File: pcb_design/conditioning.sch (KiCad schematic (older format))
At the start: 17 parts

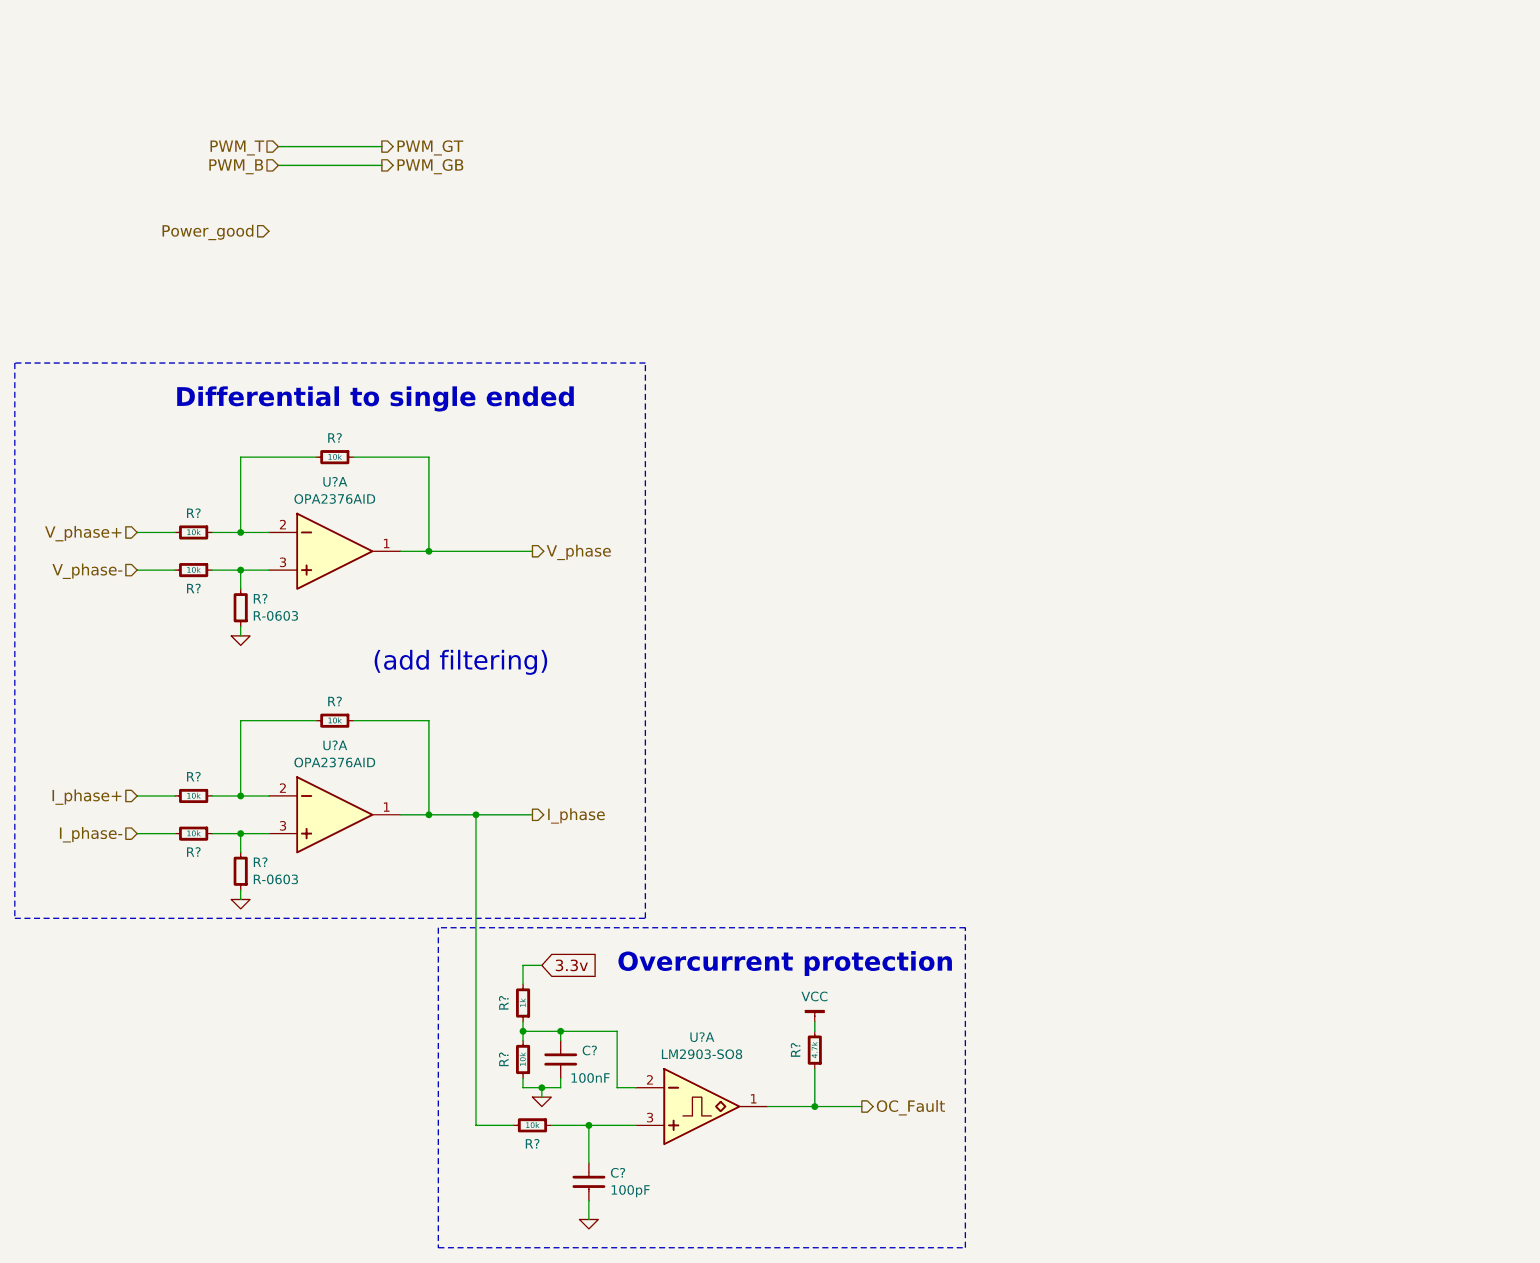
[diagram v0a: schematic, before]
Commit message: Updated MCU sheet to comply with VESC 6 pinout. Added 5v analog inputs and updated some labels
Signed-off-by: Marcos Chaparro <mchaparro@paltatech.com>
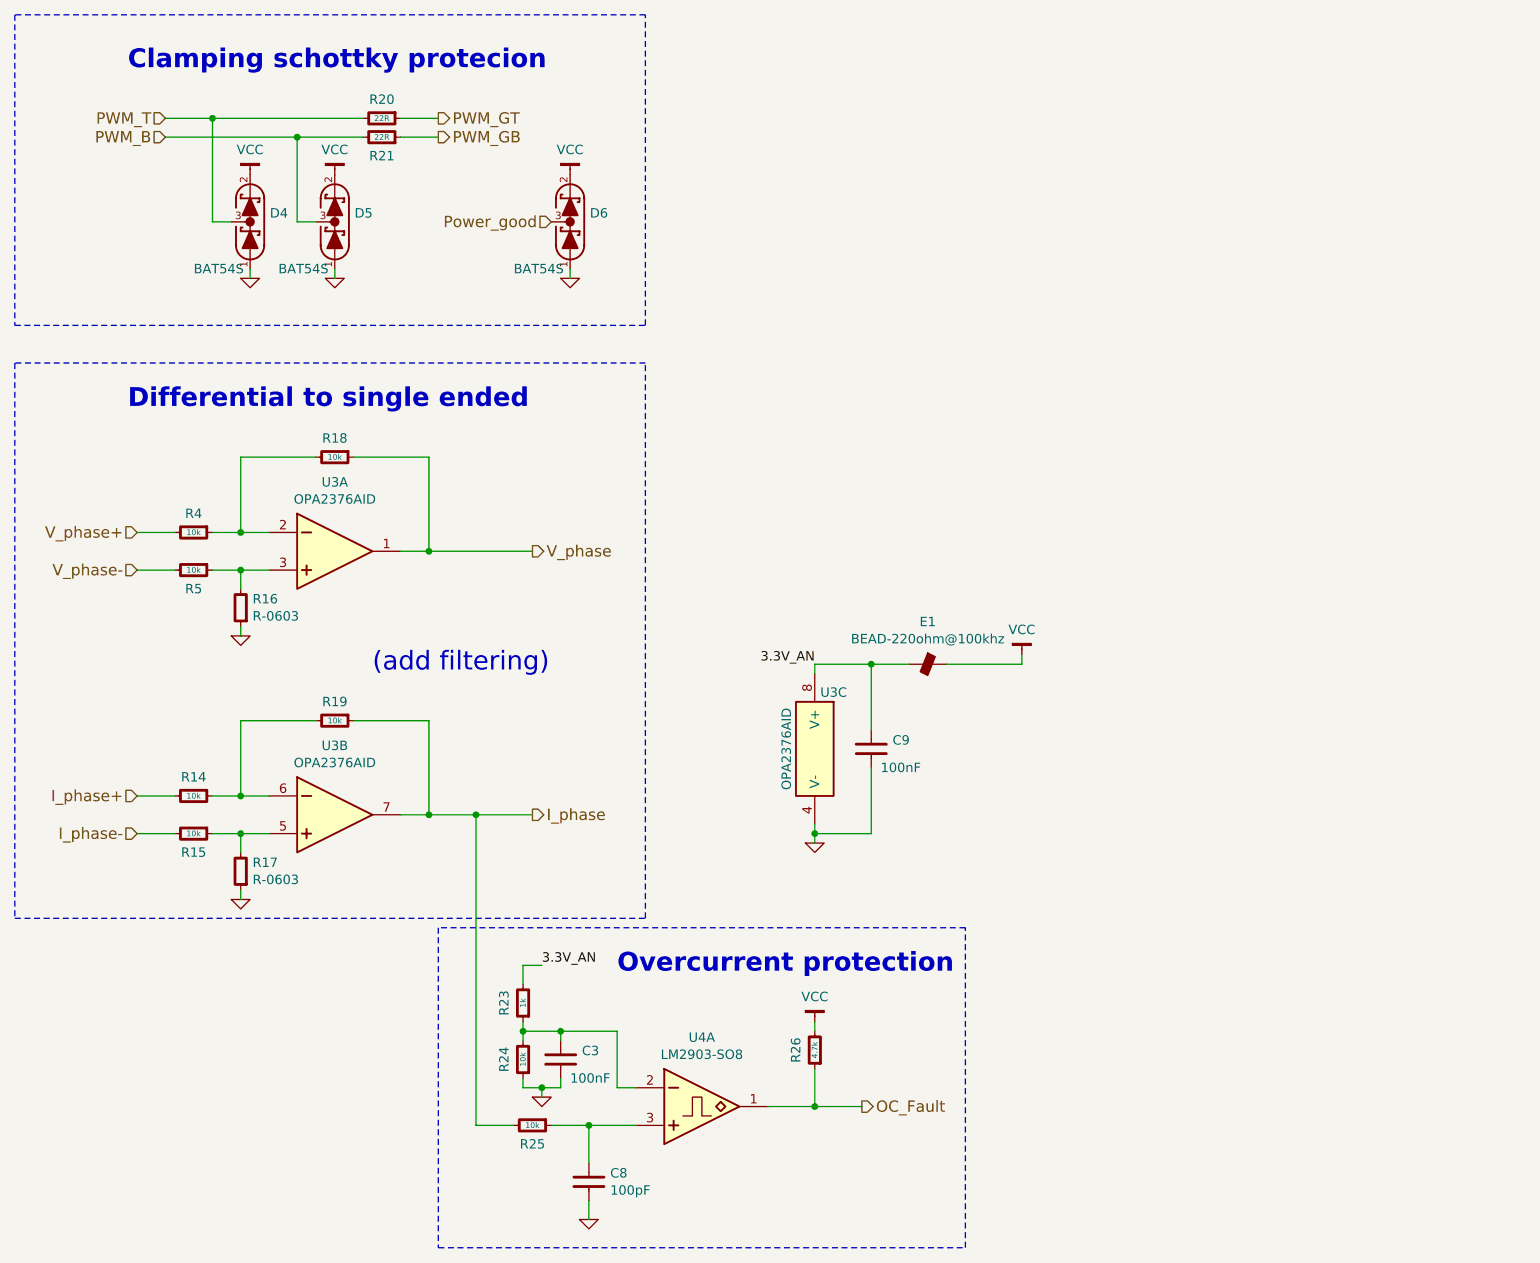
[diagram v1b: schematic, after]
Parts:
- added C9: 100nF, IPC7351-Nominal:CAPC1608X55, symbol C-0603
- added D4, D5, D6: BAT54S, smd-semi:SOT-23, symbol BAT54S
- added E1: BEAD-220ohm@100khz, IPC7351-Nominal:INDC2012X130, symbol BEAD-0805
- added R20, R21: 22R, IPC7351-Nominal:RESC1608X50, symbol R-0603
- added unit 3 of U3
- gave numbers to parts that had none: 16
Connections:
- net GND: now also C9.2, D4.1 (A), D5.1 (A), D6.1 (A), U3.4 (V-)
- net I_phase: now also U3.7 (OUT); no longer U3.1 (OUT)
- net PWM_B: now also D5.3 (COM), R21.2
- net PWM_GT: now also R20.1
- net Power_good: now also D6.3 (COM)
- net VCC: now also D4.2 (K), D5.2 (K), D6.2 (K), E1.2
- net at R14.1, R19.2: now also U3.6 (IN-); no longer U3.2 (IN-)
- net at R15.1, R17.2: now also U3.5 (IN+); no longer U3.3 (IN+)
- net 3.3v renamed 3.3V_AN
- net 3.3V_AN: now also C9.1, E1.1, U3.8 (V+)
- new net PWM_GB: R21.1
- new net PWM_T: D4.3 (COM), R20.2
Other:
- note added: "Clamping schottky protecion"

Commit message: Components placement, 3D models, updated some footprints to nominal IPC type
Signed-off-by: Marcos Chaparro <mchaparro@paltatech.com>
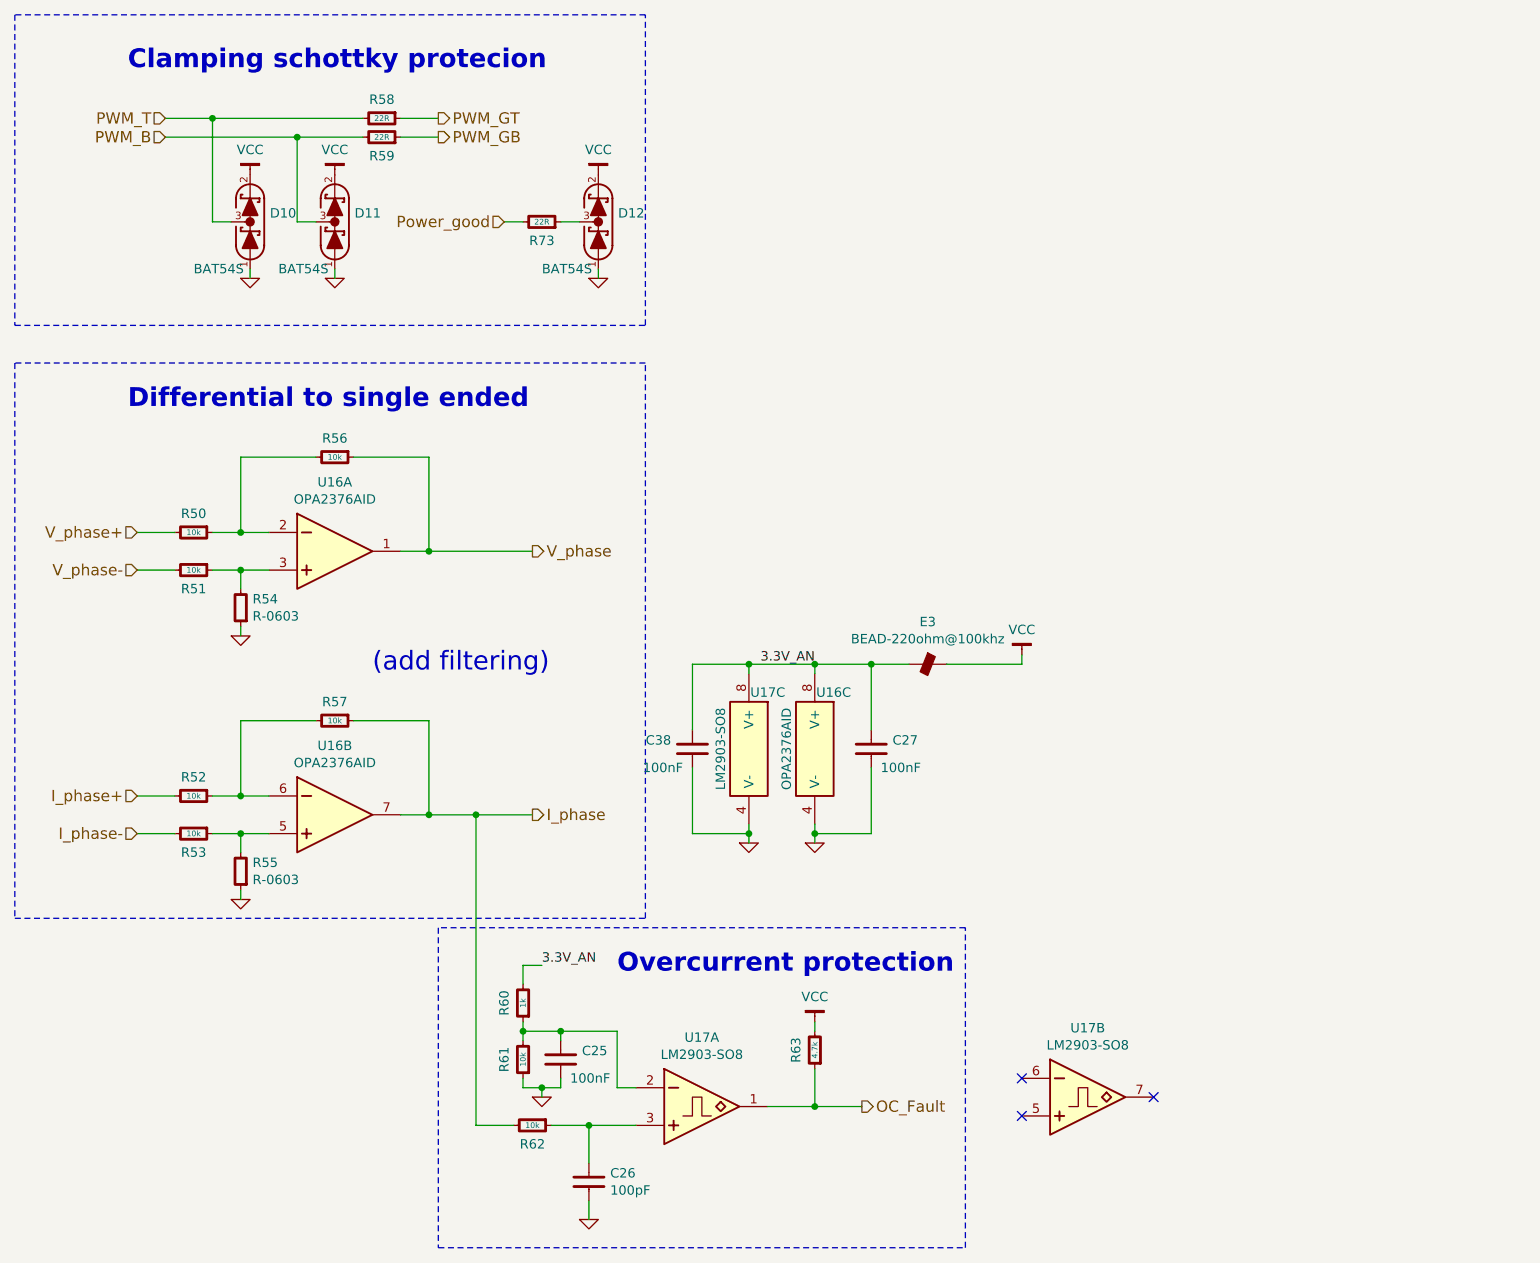
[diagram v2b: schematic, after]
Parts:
- added C36: 100nF, IPC7351-Nominal:CAPC1608X55, symbol C-0603
- added R71: 22R, IPC7351-Nominal:RESC1608X50, symbol R-0603
- added unit 3 of U4
- added unit 2 of U4
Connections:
- net 3.3V_AN: now also C36.1, U4.8 (V+)
- net GND: now also C36.2, U4.4 (V-)
- net Power_good: now also R71.2; no longer D6.3 (COM)
- new net: D6.3 (COM), R71.1
- no-connect marks 0 -> 3
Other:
- moved on the sheet: D12

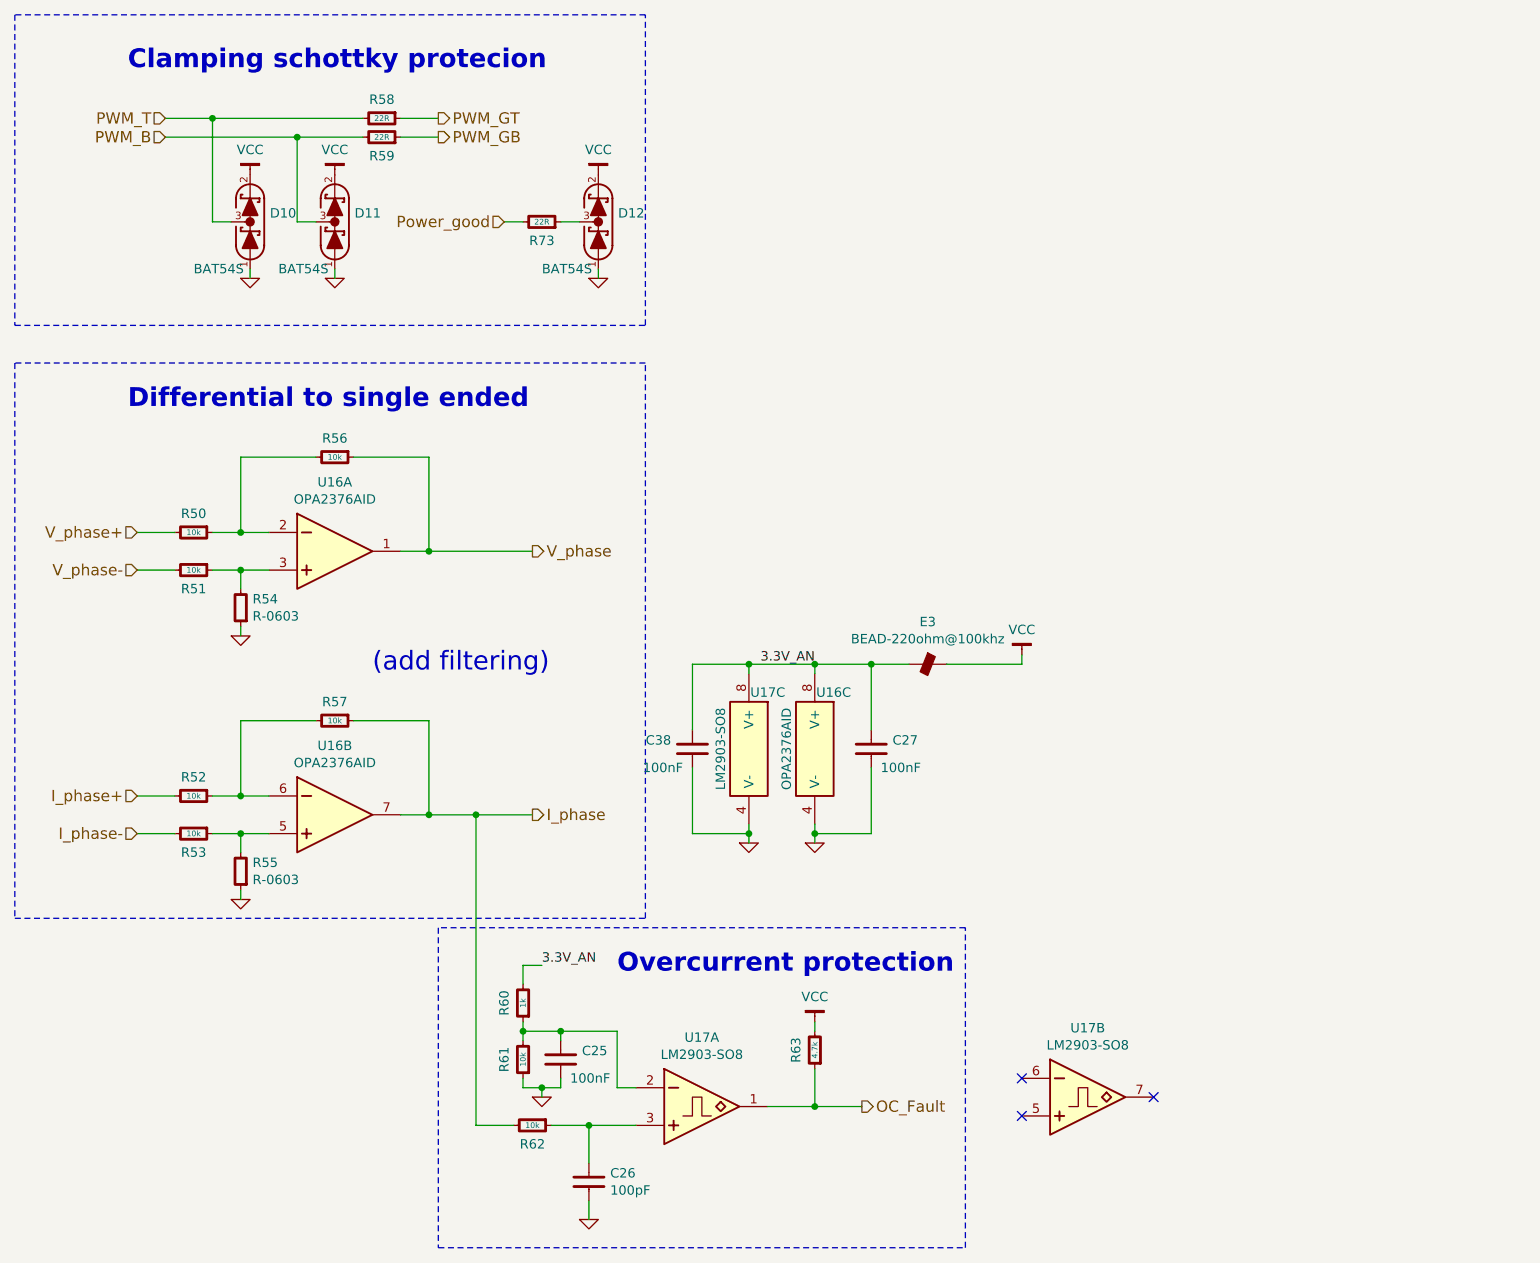
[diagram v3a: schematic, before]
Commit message: Added lp filters, fuses, tvs and power symbols
Signed-off-by: Marcos Chaparro <mchaparro@paltatech.com>
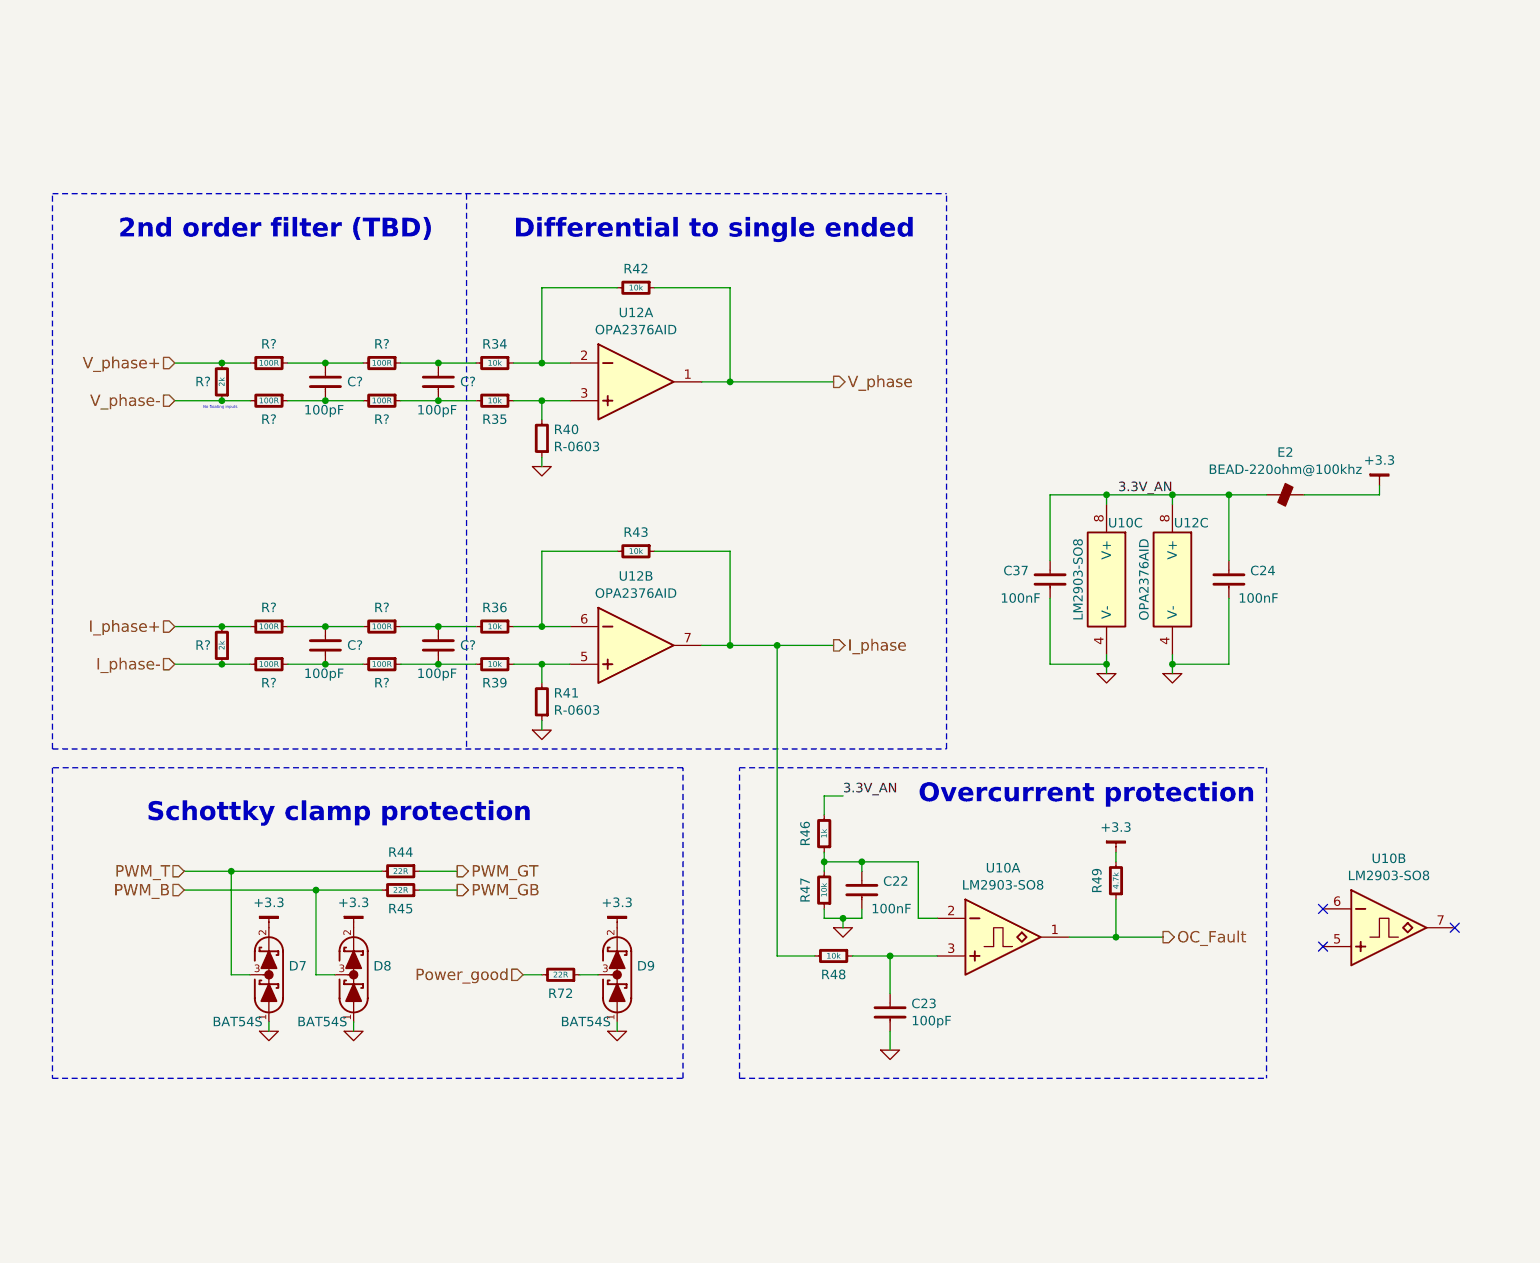
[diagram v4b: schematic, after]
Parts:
- added C? (x4): 100pF, IPC7351-Nominal:CAPC1608X55, symbol C-0603
- added R? (x8): 100R, IPC7351-Nominal:RESC1608X50, symbol R-0603
- added R? (x2): 2k, IPC7351-Nominal:RESC1608X50, symbol R-0603
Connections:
- net I_phase+: now also R?.2, R?.2; no longer R14.2
- net I_phase-: now also R?.1, R?.2; no longer R15.2
- net V_phase+: now also R?.2, R?.2; no longer R4.2
- net V_phase-: now also R?.1, R?.2; no longer R5.2
- net VCC renamed +3.3
- new net: C?.1, R4.2, R?.1
- new net: C?.2, R5.2, R?.1
- new net: C?.1, R?.1, R?.2 (x2)
- new net: C?.2, R?.1, R?.2 (x2)
- new net: C?.1, R14.2, R?.1
- new net: C?.2, R15.2, R?.1
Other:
- note added: "2nd order filter (TBD)"
- note added: "No floating inputs"
- note added: "Schottky clamp protection"
- note removed: "(add filtering)"
- note removed: "Clamping schottky protecion"
- moved on the sheet: C22, C23, C24, C37, D7, D8, D9, E2, R34, R35, R36, R39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
